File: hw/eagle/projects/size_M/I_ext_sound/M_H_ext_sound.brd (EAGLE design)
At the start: 18 parts

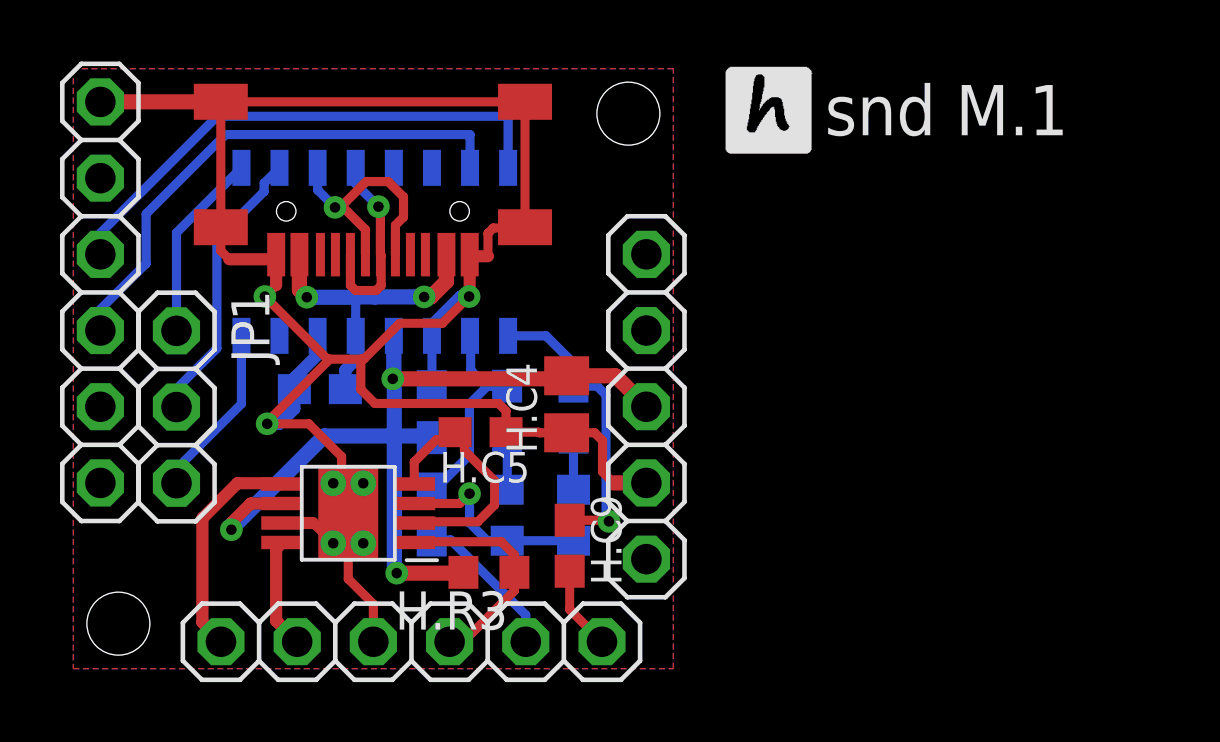
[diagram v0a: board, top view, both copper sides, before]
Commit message: updateed PCBs - adjustments based on usage of version 1
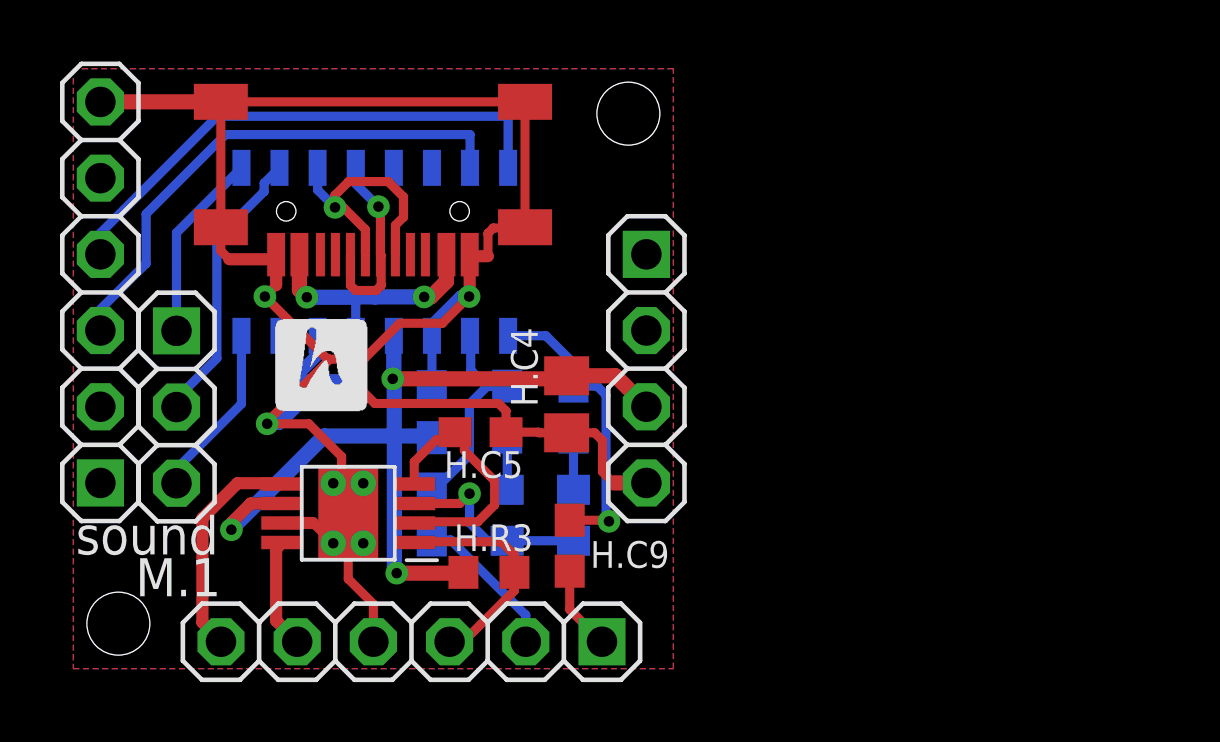
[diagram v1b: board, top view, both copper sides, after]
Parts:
- removed H.J3: (no value), pinhead2:1X05
- added JP2: (no value), pinhead2:1X04
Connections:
- net GND: now also JP2.4; no longer H.J3.4
- net VCC: now also JP2.3; no longer H.J3.3
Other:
- board text added: "sound M.1"
- board text removed: "snd M.1"
